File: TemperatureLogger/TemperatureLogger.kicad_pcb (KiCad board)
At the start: 2 copper layers, 92.5 x 119.5 mm, 127 parts, among them J1 OUTPUT, J2 OUTPUT, J3 USB_C_Receptacle_USB2.0, J4 Conn_02x03_Odd_Even, J5 Conn_02x03_Odd_Even, J6 TC_BLOCK, J7 TC_BLOCK, J8 TC_BLOCK, J9 TC_BLOCK, K1 G6E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

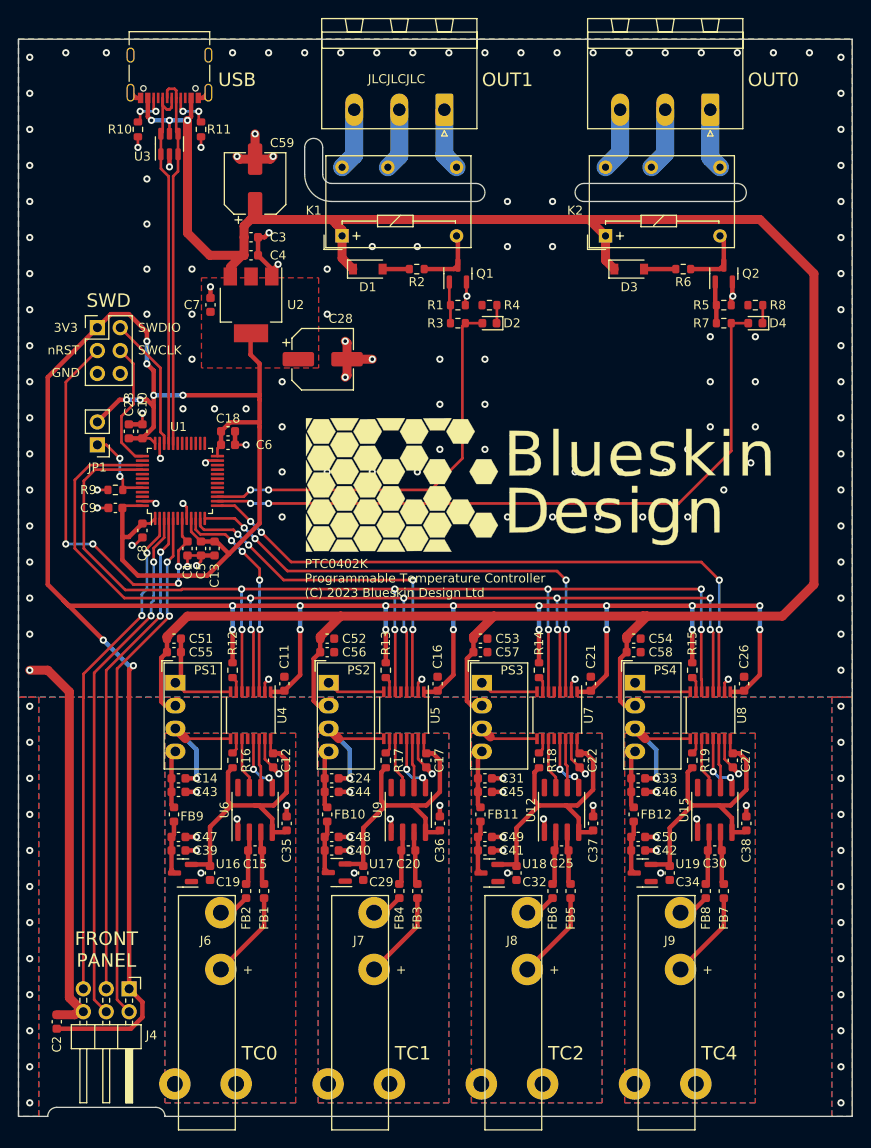
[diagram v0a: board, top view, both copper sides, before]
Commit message: added external flash and corrected issue with output disable for digital isolators
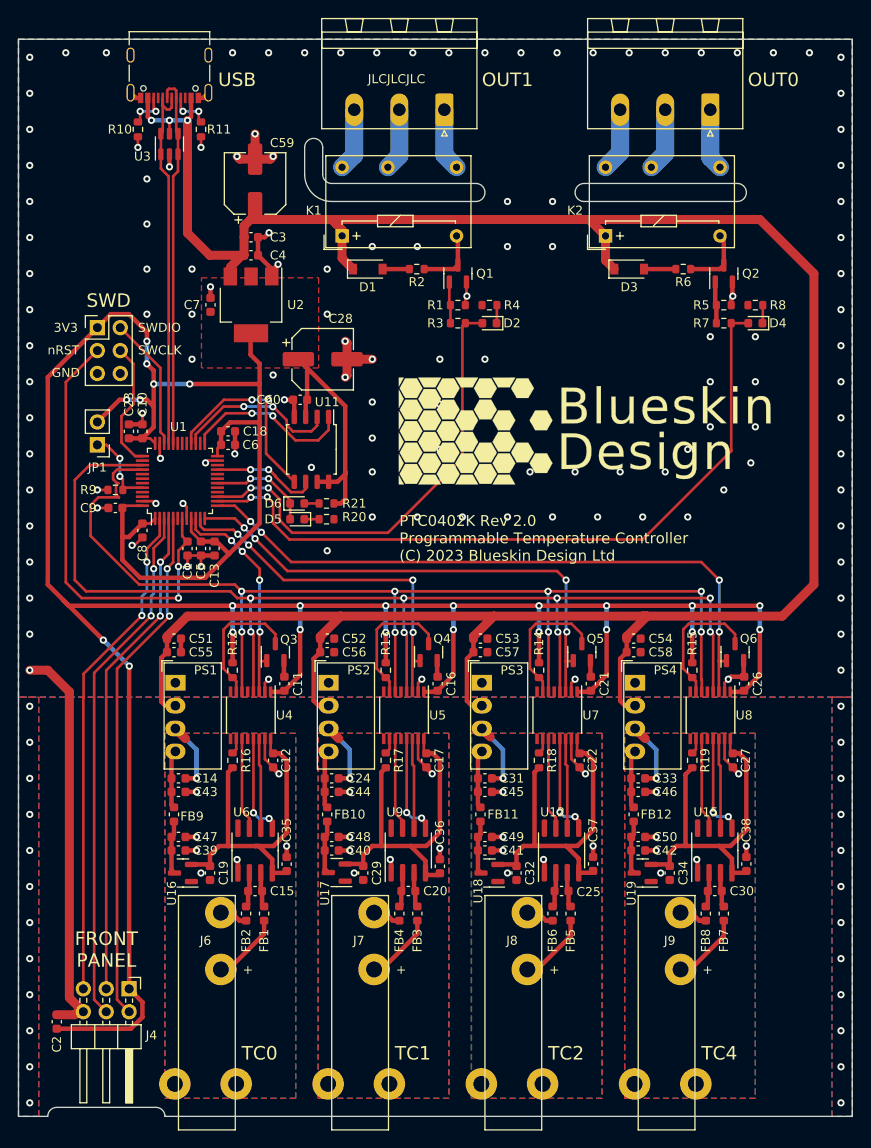
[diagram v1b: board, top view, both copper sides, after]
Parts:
- added C60: 100n, Capacitor_SMD:C_0603_1608Metric, F.Cu at (67.0, 102.0)
- added D5: LED_RED, LED_SMD:LED_0603_1608Metric, F.Cu at (66.7, 115.2)
- added D6: LED_GREEN, LED_SMD:LED_0603_1608Metric, F.Cu at (66.7, 113.5)
- added Q3: Q_NMOS_GSD, Package_TO_SOT_SMD:SOT-23, F.Cu at (64.2, 130.0)
- added Q4: Q_NMOS_GSD, Package_TO_SOT_SMD:SOT-23, F.Cu at (81.2, 130.0)
- added Q5: Q_NMOS_GSD, Package_TO_SOT_SMD:SOT-23, F.Cu at (98.2, 130.0)
- added Q6: Q_NMOS_GSD, Package_TO_SOT_SMD:SOT-23, F.Cu at (115.2, 130.0)
- added R20: 620, Resistor_SMD:R_0603_1608Metric, F.Cu at (69.9, 115.2)
- added R21: 620, Resistor_SMD:R_0603_1608Metric, F.Cu at (69.9, 113.5)
- added U11: W25Q128JV, Package_SO:SOIC-8_5.275x5.275mm_P1.27mm, F.Cu at (68.2, 107.5)
- moved C36 4.75 mm to (82.5, 153.8)
- moved C15 4.51 mm to (62.0, 156.5)
- moved C35 4.51 mm to (65.5, 153.5)
- moved U6 4.51 mm to (62.0, 152.0)
- moved C20 4.50 mm to (79.0, 156.5)
- moved C25 4.50 mm to (96.0, 156.5)
- moved C30 4.50 mm to (113.0, 156.5)
- moved C38 4.50 mm to (116.5, 153.5)
- moved U15 4.50 mm to (113.0, 152.0)
- moved U9 4.50 mm to (79.0, 152.0)
- moved C37 4.50 mm to (99.5, 153.5)
- moved U12 4.50 mm to (96.0, 152.0)
- moved FB1 2.50 mm to (63.0, 159.0)
- moved FB2 2.50 mm to (61.0, 159.0)
- moved FB3 2.50 mm to (80.0, 159.0)
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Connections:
- U1 pad 18: unconnected-(U1-PB0-Pad18) -> /LED_DEBUG
- U1 pad 21: unconnected-(U1-PB10-Pad21) -> /MEM_SCK
- U1 pad 25: unconnected-(U1-PB12-Pad25) -> /MEM_CS
- U1 pad 27: unconnected-(U1-PB14-Pad27) -> /MEM_MISO
- U1 pad 28: unconnected-(U1-PB15-Pad28) -> /MEM_MOSI
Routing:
- net +3.3V: track 352.3 -> 381.3 mm
- net /MEM_MOSI: track 0.00 -> 21.8 mm, vias 0 -> 2
- net /MEM_CS: track 0.00 -> 18.9 mm, vias 0 -> 2
- net /MEM_MISO: track 0.00 -> 18.3 mm, vias 0 -> 2
- net GND: track 137.2 -> 119.8 mm, vias 162 -> 159
- net Net-(Q4-D): track 1.75 -> 15.1 mm
- net Net-(Q6-D): track 1.75 -> 15.1 mm
- net Net-(Q3-D): track 1.75 -> 15.0 mm
- net Net-(Q5-D): track 1.75 -> 15.0 mm
- net /MEM_SCK: track 0.00 -> 11.8 mm, vias 0 -> 2
- net /LED_DEBUG: track 0.00 -> 11.4 mm, vias 0 -> 2
- net /TC_Channel2/SCKISO: track 6.01 -> 11.7 mm
- net /OUT1: track 46.0 -> 51.4 mm
- net /TC_Channel3/3V3ISO: track 32.3 -> 37.8 mm
- net /TC_Channel1/3V3ISO: track 32.7 -> 38.1 mm
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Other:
- board text added: "PTC0402K Rev 2.0 Programmable Temperature Controller (C) 2023 Blueskin Design Ltd"
- board text removed: "PTC0402K Programmable Temperature Controller (C) 2023 Blueskin Design Ltd"
